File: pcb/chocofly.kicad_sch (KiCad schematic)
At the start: 192 parts, among them P1 battery+, P2 battery-, SW1 SW_Push, SW11 SW_Push, SW12 SW_Push, SW13 SW_Push, SW14 SW_Push, SW15 SW_Push, SW16 SW_Push, SW17 SW_Push, SW18 SW_Push, SW19 SW_Push, SW2 SW_Push, SW20 SW_Push, SW21 SW_Push, SW22 SW_Push, SW23 SW_Push, SW24 SW_Push, SW25 SW_Push, SW26 SW_Push, SW27 SW_Push, SW28 SW_Push, SW29 SW_Push, SW3 SW_Push, SW30 SW_Push, SW31 SW_Push, SW32 SW_Push, SW33 SW_Push, SW34 SW_Push, SW35 SW_Push, SW36 SW_Push, SW37 SW_Push, SW38 SW_Push, SW39 SW_Push, SW4 SW_Push, SW40 SW_Push, SW41 SW_Push, SW42 SW_Push, SW43 SW_Push, SW44 SW_Push, SW45 SW_Push, SW46 SW_Push, SW47 SW_Push, SW48 SW_Push, SW49 SW_Push, SW5 SW_Push, SW50 SW_Push, SW51 SW_Push, SW52 SW_Push, SW53 SW_Push, SW54 SW_Push, SW55 SW_Push, SW56 SW_Push, SW57 SW_Push, SW58 SW_Push, SW59 SW_Push, SW6 SW_Push, SW60 SW_Push, SW61 SW_Push, SW62 Reset, SW63 Power, SW7 SW_Push, SW8 SW_Push, SW9 SW_Push

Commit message: wip
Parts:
- SW1, SW11, SW12, SW13, SW14, SW15, SW16, SW17, SW18, SW19, SW2, SW20, SW21, SW22, SW23, SW24, SW25, SW26, SW27, SW28, SW29, SW3, SW30, SW31, SW32, SW33, SW34, SW35, SW36, SW37, SW38, SW39, SW4, SW40, SW41, SW42, SW43, SW44, SW45, SW46, SW47, SW48, SW49, SW5, SW50, SW51, SW52, SW53, SW54, SW55, SW56, SW57, SW58, SW59, SW6, SW60, SW61, SW7, SW8, SW9: footprint footprints:Kailh_socket_PG1350_optional_mkultra -> footprints:Kailh_socket_PG1350_chosfox_17_5mm

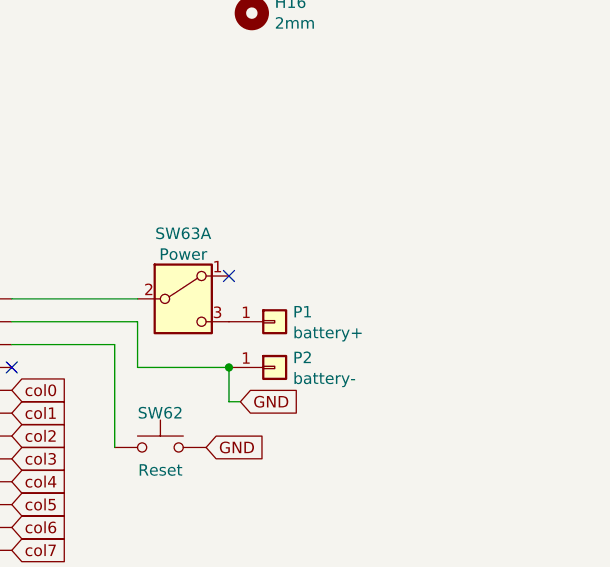
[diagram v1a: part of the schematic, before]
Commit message: added secondary power switch
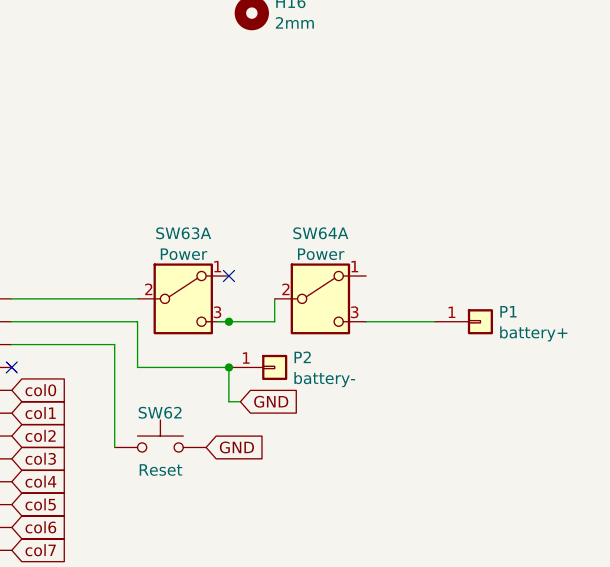
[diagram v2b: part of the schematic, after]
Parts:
- added SW64: Power, footprints:Switch_MSK-12C01-07, symbol Switch:SW_DPDT_x2
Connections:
- net at P1.1 (Pin_1): now also SW64.3 (C); no longer SW63.3 (C)
- new net: SW63.3 (C), SW64.2 (B)
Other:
- moved on the sheet: P1
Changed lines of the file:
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@@
 	)
 	(junction
+		(at 242.57 96.52)
+		(diameter 0)
+		(color 0 0 0 0)
+	)
+	(junction
 		(at 128.27 102.87)
 		(diameter 0)
@@
 	(wire
 		(pts
+			(xy 247.65 96.52) (xy 247.65 93.98)
+		)
+		(stroke
+			(width 0)
+			(type default)
+		)
+	)
+	(wire
+		(pts
 			(xy 132.08 171.45) (xy 146.05 171.45)
 		)
@@
 	(wire
 		(pts
+			(xy 241.3 96.52) (xy 242.57 96.52)
+		)
+		(stroke
+			(width 0)
+			(type default)
+		)
+	)
+	(wire
+		(pts
 			(xy 156.21 87.63) (xy 156.21 102.87)
 		)
@@
 	(wire
 		(pts
+			(xy 257.81 96.52) (xy 265.43 96.52)
+		)
+		(stroke
+			(width 0)
+			(type default)
+		)
+	)
+	(wire
+		(pts
 			(xy 34.29 125.73) (xy 48.26 125.73)
 		)
@@
 	(wire
 		(pts
+			(xy 242.57 96.52) (xy 247.65 96.52)
+		)
+		(stroke
+			(width 0)
+			(type default)
+		)
+	)
+	(wire
+		(pts
 			(xy 121.92 29.21) (xy 120.65 29.21)
 		)
@@
 	(symbol
 		(lib_id "chocofly-rescue:i2c_pin-pin_pad")
-		(at 247.65 96.52 0)
+		(at 270.51 96.52 0)
 		(unit 1)
 		(exclude_from_sim no)
@@
 		(dnp no)
 		(property "Reference" "P1"
-			(at 249.682 95.4532 0)
+			(at 272.542 95.4532 0)
 			(effects
 				(font
@@
 		)
 		(property "Value" "battery+"
-			(at 249.682 97.7646 0)
+			(at 272.542 97.7646 0)
 			(effects
 				(font
@@
 		)
 		(property "Footprint" "footprints:1pin_conn"
-			(at 247.65 96.52 0)
+			(at 270.51 96.52 0)
 			(effects
 				(font
@@
 		)
 		(property "Datasheet" ""
-			(at 247.65 96.52 0)
+			(at 270.51 96.52 0)
 			(effects
 				(font
@@
 		)
 		(property "Description" ""
-			(at 247.65 96.52 0)
+			(at 270.51 96.52 0)
 			(effects
 				(font
@@
 					(unit 1)
 				)
+			)
+		)
+	)
+	(symbol
+		(lib_id "Switch:SW_DPDT_x2")
+		(at 252.73 93.98 0)
+		(unit 1)
+		(exclude_from_sim no)
+		(in_bom yes)
+		(on_board yes)
+		(dnp no)
+		(property "Reference" "SW64"
+			(at 252.73 86.741 0)
+			(effects
+				(font
+					(size 1.27 1.27)
+				)
+			)
+		)
+		(property "Value" "Power"
+			(at 252.73 89.0524 0)
+			(effects
+				(font
+					(size 1.27 1.27)
+				)
+			)
+		)
+		(property "Footprint" "footprints:Switch_MSK-12C01-07"
+			(at 252.73 93.98 0)
+			(effects
+				(font
+					(size 1.27 1.27)
+				)
+				(hide yes)
+			)
+		)
+		(property "Datasheet" "~"
+			(at 252.73 93.98 0)
+			(effects
+				(font
+					(size 1.27 1.27)
+				)
+				(hide yes)
+			)
+		)
+		(property "Description" ""
+			(at 252.73 93.98 0)
+			(effects
+				(font
+					(size 1.27 1.27)
+				)
+				(hide yes)
+			)
+		)
+		(pin "1"
+		)
+		(pin "2"
+		)
+		(pin "3"
+		)
+		(pin "4"
+		)
+		(pin "5"
+		)
+		(pin "6"
+		)
+		(instances
+			(project "chocofly"
+				(path "/db4dac64-1581-426b-b2ad-fbb21197bc47"
+					(reference "SW64")
+					(unit 1)
+				)

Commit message: checks ok
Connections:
- net encA: now also ENC1.A, JP1.1
- net encB: now also ENC1.B, JP2.1
- net at P1.1 (Pin_1), SW64.3 (C): now also SW63.3 (C)
- net at MCU1.24 (RAW), SW63.2 (B): now also SW64.2 (B)
- no-connect marks 5 -> 6
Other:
- moved on the sheet: SW64A
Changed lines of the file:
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@@
 	)
 	(junction
-		(at 242.57 96.52)
-		(diameter 0)
-		(color 0 0 0 0)
-	)
-	(junction
 		(at 128.27 102.87)
 		(diameter 0)
@@
 	)
 	(junction
+		(at 68.58 21.59)
+		(diameter 0)
+		(color 0 0 0 0)
+	)
+	(junction
 		(at 48.26 80.01)
 		(diameter 0)
@@
 	)
 	(junction
+		(at 68.58 19.05)
+		(diameter 0)
+		(color 0 0 0 0)
+	)
+	(junction
 		(at 86.36 133.35)
 		(diameter 0)
@@
 	)
 	(junction
+		(at 231.14 93.98)
+		(diameter 0)
+		(color 0 0 0 0)
+	)
+	(junction
 		(at 156.21 72.39)
 		(diameter 0)
@@
 	)
 	(junction
+		(at 73.66 19.05)
+		(diameter 0)
+		(color 0 0 0 0)
+	)
+	(junction
 		(at 48.26 156.21)
 		(diameter 0)
@@
 	)
 	(junction
+		(at 73.66 21.59)
+		(diameter 0)
+		(color 0 0 0 0)
+	)
+	(junction
 		(at 114.3 87.63)
 		(diameter 0)
@@
 	)
 	(junction
+		(at 259.08 96.52)
+		(diameter 0)
+		(color 0 0 0 0)
+	)
+	(junction
 		(at 114.3 102.87)
 		(diameter 0)
@@
 	)
 	(no_connect
+		(at 242.57 78.74)
+	)
+	(no_connect
 		(at 128.27 34.29)
 	)
@@
 	(wire
 		(pts
-			(xy 247.65 96.52) (xy 247.65 93.98)
-		)
-		(stroke
-			(width 0)
-			(type default)
-		)
-	)
-	(wire
-		(pts
 			(xy 132.08 171.45) (xy 146.05 171.45)
 		)
@@
 	(wire
 		(pts
-			(xy 241.3 96.52) (xy 242.57 96.52)
+			(xy 156.21 87.63) (xy 156.21 102.87)
 		)
 		(stroke
@@
 	(wire
 		(pts
-			(xy 156.21 87.63) (xy 156.21 102.87)
+			(xy 259.08 96.52) (xy 265.43 96.52)
 		)
 		(stroke
@@
 	(wire
 		(pts
+			(xy 62.23 19.05) (xy 68.58 19.05)
+		)
+		(stroke
+			(width 0)
+			(type default)
+		)
+	)
+	(wire
+		(pts
 			(xy 27.94 64.77) (xy 34.29 64.77)
 		)
@@
 	(wire
 		(pts
+			(xy 231.14 81.28) (xy 231.14 93.98)
+		)
+		(stroke
+			(width 0)
+			(type default)
+		)
+	)
+	(wire
+		(pts
+			(xy 231.14 93.98) (xy 218.44 93.98)
+		)
+		(stroke
+			(width 0)
+			(type default)
+		)
+	)
+	(wire
+		(pts
 			(xy 132.08 110.49) (xy 146.05 110.49)
 		)
@@
 	(wire
 		(pts
+			(xy 242.57 96.52) (xy 259.08 96.52)
+		)
+		(stroke
+			(width 0)
+			(type default)
+		)
+	)
+	(wire
+		(pts
 			(xy 62.23 95.25) (xy 76.2 95.25)
 		)
@@
 	(wire
 		(pts
+			(xy 232.41 81.28) (xy 231.14 81.28)
+		)
+		(stroke
+			(width 0)
+			(type default)
+		)
+	)
+	(wire
+		(pts
 			(xy 48.26 80.01) (xy 62.23 80.01)
 		)
@@
 	(wire
 		(pts
-			(xy 257.81 96.52) (xy 265.43 96.52)
+			(xy 242.57 83.82) (xy 259.08 83.82)
 		)
 		(stroke
@@
 	(wire
 		(pts
+			(xy 68.58 19.05) (xy 73.66 19.05)
+		)
+		(stroke
+			(width 0)
+			(type default)
+		)
+	)
+	(wire
+		(pts
 			(xy 58.42 148.59) (xy 58.42 163.83)
 		)
@@
 	(wire
 		(pts
+			(xy 259.08 83.82) (xy 259.08 96.52)
+		)
+		(stroke
+			(width 0)
+			(type default)
+		)
+	)
+	(wire
+		(pts
+			(xy 62.23 21.59) (xy 68.58 21.59)
+		)
+		(stroke
+			(width 0)
+			(type default)
+		)
+	)
+	(wire
+		(pts
 			(xy 44.45 49.53) (xy 44.45 57.15)
 		)
@@
 	(wire
 		(pts
-			(xy 232.41 93.98) (xy 218.44 93.98)
+			(xy 232.41 93.98) (xy 231.14 93.98)
+		)
+		(stroke
+			(width 0)
+			(type default)
+		)
+	)
+	(wire
+		(pts
+			(xy 68.58 21.59) (xy 73.66 21.59)
 		)
 		(stroke
@@
 	(wire
 		(pts
-			(xy 242.57 96.52) (xy 247.65 96.52)
-		)
-		(stroke
-			(width 0)
-			(type default)
-		)
-	)
-	(wire
-		(pts
 			(xy 121.92 29.21) (xy 120.65 29.21)
 		)
@@
 	(global_label "encA"
 		(shape input)
-		(at 68.58 19.05 180)
+		(at 62.23 19.05 180)
 		(effects
 			(font
@@
 		)
 		(property "Intersheetrefs" "${INTERSHEET_REFS}"
-			(at 68.58 19.05 0)
+			(at 62.23 19.05 0)
 			(effects
 				(font
@@
 	(global_label "encB"
 		(shape input)
-		(at 68.58 21.59 180)
+		(at 62.23 21.59 180)
 		(effects
 			(font
@@
 		)
 		(property "Intersheetrefs" "${INTERSHEET_REFS}"
-			(at 68.58 21.59 0)
+			(at 62.23 21.59 0)
 			(effects
 				(font
@@
 	(symbol
 		(lib_id "Switch:SW_DPDT_x2")
-		(at 252.73 93.98 0)
+		(at 237.49 81.28 0)
 		(unit 1)
 		(exclude_from_sim no)
@@
 		(dnp no)
 		(property "Reference" "SW64"
-			(at 252.73 86.741 0)
+			(at 237.49 74.041 0)
 			(effects
 				(font
@@
 		)
 		(property "Value" "Power"
-			(at 252.73 89.0524 0)
+			(at 237.49 76.3524 0)
 			(effects
 				(font
@@
 		)
 		(property "Footprint" "footprints:Switch_MSK-12C01-07"
-			(at 252.73 93.98 0)
+			(at 237.49 81.28 0)
 			(effects
 				(font
@@
 		)
 		(property "Datasheet" "~"
-			(at 252.73 93.98 0)
+			(at 237.49 81.28 0)
 			(effects
 				(font
@@
 		)
 		(property "Description" ""
-			(at 252.73 93.98 0)
+			(at 237.49 81.28 0)
 			(effects
 				(font

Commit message: fix
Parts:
- removed H1, H17, H20, H30, H31, H32, H33, H34, H35, H4, H5, H6: 5mm, footprints:hole_5mm, symbol Mechanical:MountingHole
- removed H10, H11, H12, H15, H16, H18, H42, H43, H46, H9: 2mm, footprints:hole_2mm, symbol Mechanical:MountingHole
- removed H13, H14, H48, H49, H50, H51, H67: 1mm, footprints:hole_1mm, symbol Mechanical:MountingHole
- removed H19, H36, H37, H38, H39, H40, H41, H45, H47, H52, H53, H54, H55, H56, H57, H58, H59, H61, H62, H7, H8: 3mm, footprints:hole_3mm, symbol Mechanical:MountingHole
- removed H2, H23, H25, H26, H27, H28, H29, H3, H44: 10mm, footprints:hole_10mm, symbol Mechanical:MountingHole
